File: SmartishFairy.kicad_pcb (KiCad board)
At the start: 2 copper layers, 95 parts, among them J1 USB_BOOT, J10 Conn_01x02_Pin, J11 USB_C_Receptacle_USB2.0, J12 Conn_01x04_Pin, J13 Data_In, J14 Data_Out, J15 Ctl_Pwr, J2 Conn_ARM_JTAG_SWD_10, J3 IN1, J4 IN2, J5 IN3, J6 OUT1, J7 OUT2, J8 OUT3, J9 Conn_01x02_Pin, SW1 SW_DIP_x08, U1 RP2040, U2 W25Q128JVS, U3 NCP1117-3.3_SOT223, U4 TXB0104RGY, U5 L6226Q, U6 L6226Q, U7 L6226Q, Y1 Crystal

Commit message: Layout WIP
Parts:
- C14, C4, C8: footprint Capacitor_SMD:C_0805_2012Metric -> Capacitor_SMD:CP_Elec_5x4.4
- moved D1 99.5 mm to (261.3, 56.1)
- moved J12 78.2 mm to (154.4, 53.0)
- moved Y1 75.3 mm to (206.8, 56.5)
- moved C10 41.4 mm to (186.6, 71.8)
- moved C11 41.4 mm to (186.6, 74.8)
- moved C12 41.4 mm to (186.6, 77.8)
- moved C7 41.4 mm to (186.6, 62.8)
- moved C8 41.4 mm to (186.6, 65.8)
- moved C9 41.4 mm to (186.6, 68.8)
- moved R1 41.4 mm to (201.9, 62.8)
- moved R2 41.4 mm to (201.9, 65.7)
- moved R3 41.4 mm to (201.9, 68.7)
- moved R4 41.4 mm to (201.9, 71.6)
- moved R5 41.4 mm to (201.9, 74.6)
- moved R6 41.4 mm to (201.9, 77.5)
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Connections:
- D4 pad 1: Net-(D4-K) -> GND
- D4 pad 2: GND -> Net-(D4-A)
- D5 pad 1: Net-(D5-K) -> GND
- D5 pad 2: GND -> Net-(D5-A)
- D6 pad 1: Net-(D6-K) -> GND
- D6 pad 2: GND -> Net-(D6-A)
- D7 pad 1: Net-(D7-K) -> GND
- D7 pad 2: GND -> Net-(D7-A)
- R24 pad 2: Net-(D4-K) -> Net-(D4-A)
- R25 pad 2: Net-(D5-K) -> Net-(D5-A)
- R26 pad 2: Net-(D6-K) -> Net-(D6-A)
- R27 pad 2: Net-(D7-K) -> Net-(D7-A)

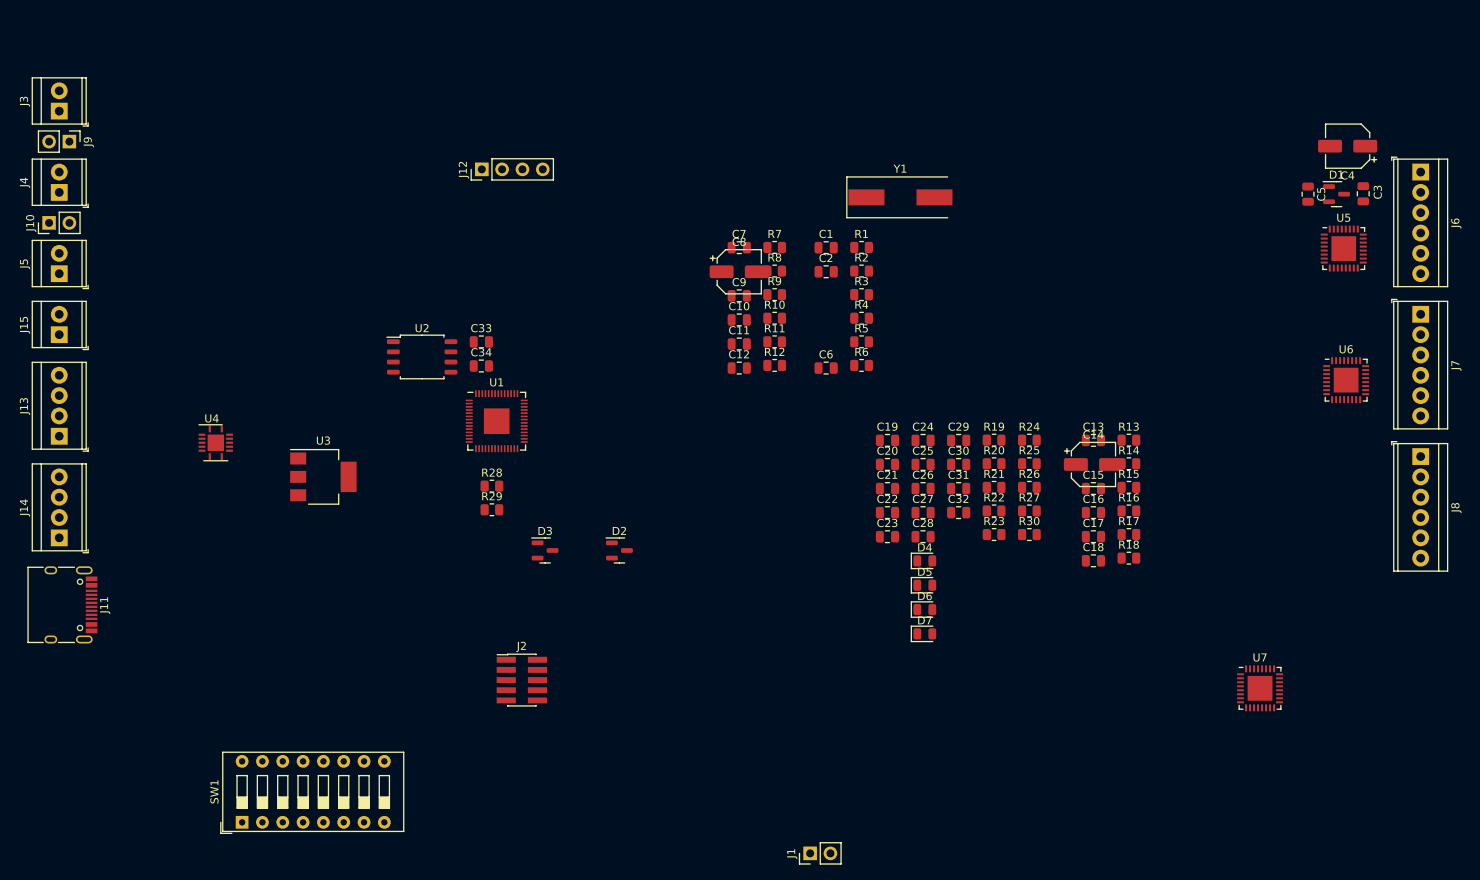
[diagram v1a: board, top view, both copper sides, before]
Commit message: Convert to KiCAD v9 and basic sort out of components
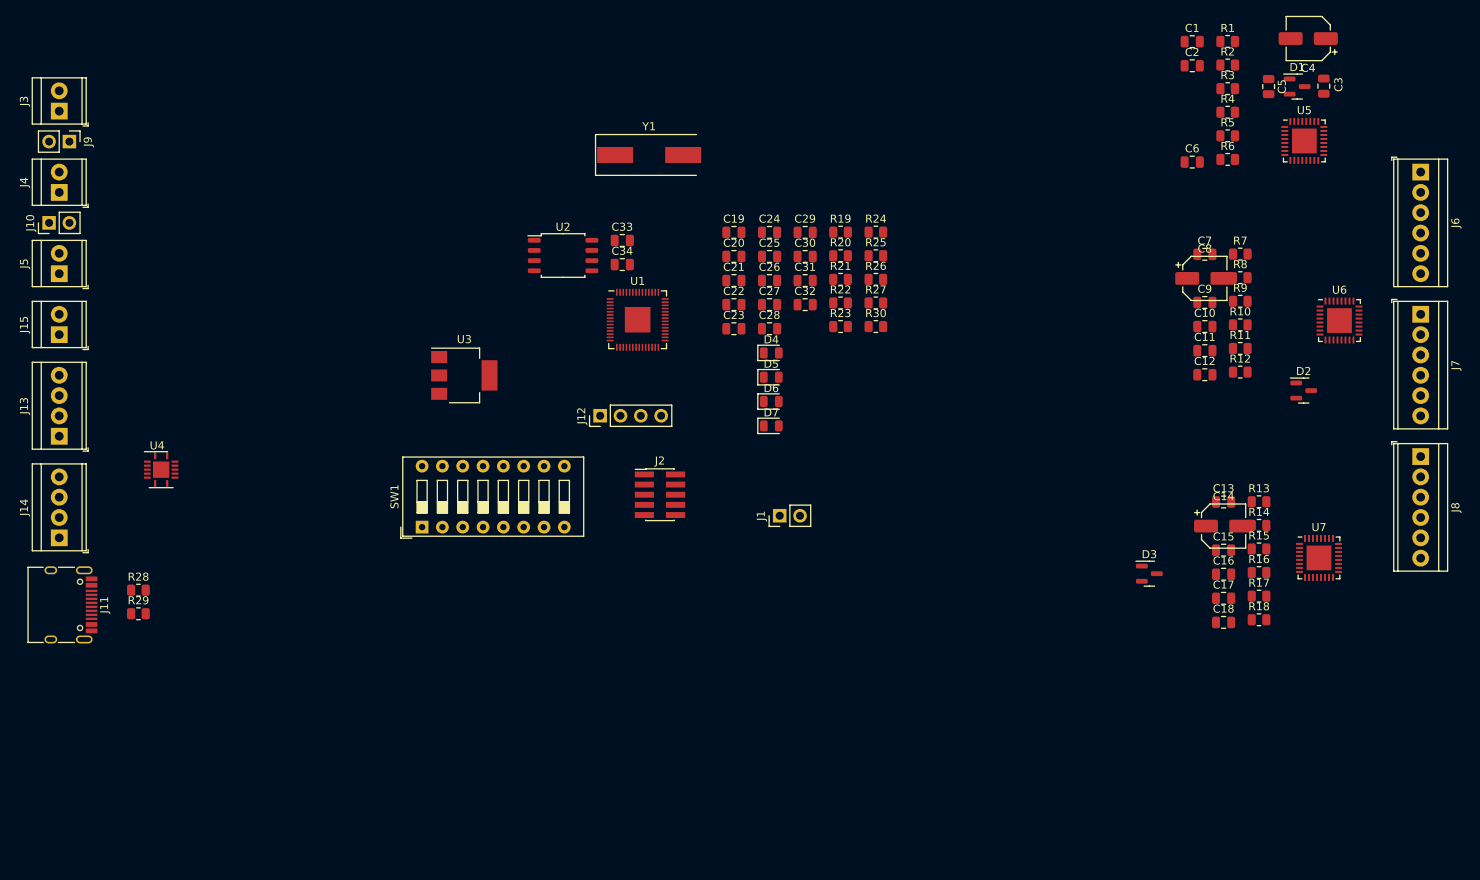
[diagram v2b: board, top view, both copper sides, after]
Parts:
- moved D2 87.8 mm to (257.2, 80.7)
- moved D3 75.6 mm to (237.9, 103.5)
- moved C10 58.2 mm to (244.8, 72.7)
- moved C11 58.2 mm to (244.8, 75.7)
- moved C12 58.2 mm to (244.8, 78.7)
- moved C7 58.2 mm to (244.8, 63.6)
- moved C8 58.2 mm to (244.8, 66.6)
- moved C9 58.2 mm to (244.8, 69.6)
- moved R10 58.2 mm to (249.2, 72.4)
- moved R11 58.2 mm to (249.2, 75.4)
- moved R12 58.2 mm to (249.2, 78.3)
- moved R7 58.2 mm to (249.2, 63.6)
- moved R8 58.2 mm to (249.2, 66.5)
- moved R9 58.2 mm to (249.2, 69.5)
- moved R6 52.5 mm to (247.7, 51.8)
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
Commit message: Additional layout
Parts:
- C1, C10, C11, C12, C13, C15, C16, C17, C18, C19, C2, C20, C21, C22, C23, C24, C25, C26, C27, C28, C29, C3, C30, C31, C32, C33, C34, C5, C6, C7, C9: footprint Capacitor_SMD:C_0805_2012Metric -> Capacitor_SMD:C_0603_1608Metric
- R1, R10, R11, R12, R13, R14, R15, R16, R17, R18, R19, R2, R20, R21, R22, R23, R24, R25, R26, R27, R28, R29, R3, R30, R4, R5, R6, R7, R8, R9: footprint Resistor_SMD:R_0805_2012Metric -> Resistor_SMD:R_0603_1608Metric
- Y1: value Crystal -> 12MHz; footprint Crystal:Crystal_SMD_HC49-SD -> Crystal:Crystal_SMD_3225-4Pin_3.2x2.5mm
- moved C3 78.4 mm to (182.9, 58.9)
- moved U6 76.0 mm to (187.1, 86.3), turned to 90 degrees
- moved R13 75.7 mm to (176.7, 105.9)
- moved R7 75.4 mm to (176.5, 83.4)
- moved R16 75.0 mm to (176.7, 108.0), turned to 180 degrees
- moved R14 74.9 mm to (176.8, 100.2)
- moved R15 74.9 mm to (176.8, 98.1), turned to 180 degrees
- moved J8 74.3 mm to (198.0, 97.5)
- moved R10 73.9 mm to (176.5, 85.5), turned to 180 degrees
- moved J7 73.9 mm to (198.0, 75.0)
- moved J6 73.8 mm to (198.0, 53.5)
- moved R8 73.5 mm to (176.5, 77.7)
- moved R1 73.3 mm to (176.3, 54.1), turned to 180 degrees
- moved C4 73.0 mm to (186.7, 53.5)
- moved R9 72.9 mm to (176.5, 75.6), turned to 180 degrees
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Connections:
- Y1 pad 1: Net-(C31-Pad1) -> Net-(U1-XIN)
- Y1 pad 2: Net-(U1-XIN) -> GND
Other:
- board outline added: 95 x 69 mm

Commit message: Added optional pull up resistor for flash chip
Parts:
- added R31: DNF, Resistor_SMD:R_0603_1608Metric, F.Cu at (143.7, 83.3)
- moved J1 33.3 mm to (140.8, 83.5), turned to 0 degrees
- moved R21 24.6 mm to (143.7, 86.5), turned to 90 degrees
- moved C29 19.4 mm to (147.6, 64.1), turned to 90 degrees
- moved C25 17.6 mm to (149.2, 76.7)
- moved U4 15.5 mm to (121.2, 91.2)
- moved C34 10.9 mm to (143.7, 101.2)
- moved C33 10.9 mm to (131.5, 99.8)
- moved U3 10.9 mm to (137.5, 99.0)
- moved C24 10.5 mm to (156.3, 68.2), turned to 90 degrees
- moved J2 8.18 mm to (158.3, 109.8)
- moved C26 4.21 mm to (169.0, 73.1)
- moved C32 2.51 mm to (143.7, 80.2)
- moved U2 2.51 mm to (147.6, 83.3)
- moved C20 0.77 mm to (159.2, 81.3)

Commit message: More updates
Placed more components
Updated 3D models
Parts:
- added H1: MountingHole, MountingHole:MountingHole_3mm, F.Cu at (112.0, 112.0)
- added H2: MountingHole, MountingHole:MountingHole_3mm, F.Cu at (198.0, 112.0)
- added H3: MountingHole, MountingHole:MountingHole_3mm, F.Cu at (198.0, 51.0)
- added H4: MountingHole, MountingHole:MountingHole_3mm, F.Cu at (112.0, 51.0)
- C19, C20, C21, C22, C23, C24, C25, C26, C27, C28, C29, C32: footprint Capacitor_SMD:C_0603_1608Metric -> Capacitor_SMD:C_0402_1005Metric
- C30, C31: value 27pF -> 15pF; footprint Capacitor_SMD:C_0603_1608Metric -> Capacitor_SMD:C_0402_1005Metric
- R19, R20, R21, R22, R23, R24, R25, R26, R27, R28, R29, R30, R31: footprint Resistor_SMD:R_0603_1608Metric -> Resistor_SMD:R_0402_1005Metric
- Y1: value 12MHz -> ABM8-272-T3
- moved C23 30.5 mm to (139.8, 70.8), turned to 180 degrees
- moved C27 28.2 mm to (142.9, 64.2), turned to 90 degrees
- moved C26 26.5 mm to (144.0, 64.2), turned to 90 degrees
- moved C28 23.9 mm to (143.5, 76.3), turned to 180 degrees
- moved C20 21.6 mm to (139.8, 71.8), turned to 180 degrees
- moved J6 17.0 mm to (198.0, 70.5), turned to 90 degrees
- moved C21 16.5 mm to (153.9, 69.5)
- moved J7 13.0 mm to (198.0, 88.0), turned to 90 degrees
- moved J11 12.4 mm to (125.2, 111.5), turned to 0 degrees
- moved R29 8.76 mm to (124.2, 101.0), turned to 90 degrees
- moved J10 8.21 mm to (122.0, 71.5)
- moved J9 8.21 mm to (122.0, 62.0)
- moved J8 8.00 mm to (198.0, 105.5), turned to 90 degrees
- moved R28 5.94 mm to (127.2, 101.0), turned to 90 degrees
- moved J4 4.47 mm to (112.0, 65.0), turned to -90 degrees
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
